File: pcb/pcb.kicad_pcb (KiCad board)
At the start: 2 copper layers, 84.6 x 82.7 mm, 329 parts, among them J1 SMA, J2 SMA, J3 SMA, P1 CONN_02X03, P10 TST, P11 EPV, P12 EPV, P2 A1, P3 SWD, P4 SWC, P5 USB_OTG, P6 CONN_02X03, P7 EPV, P8 TST, P9 TST, Q1 2N7000, Q2 BF861, U1 LM7705, U10 TPS77001DBVT, U11 AD829, U12 AD8061, U13 AD8031, U2 MAX4477, U3 NCP700B, U4 MAX11102, U5 MAX6126BASA25+, U6 STM32F302KxU, U7 NCP700B, U8 501HCA12M0000DAG, U9 LT3571

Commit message: pcb: Update to v1.1
Changes:
 Add input protection diodes to acquisition board
 Add second screw hole to the preamplifier
 Add PCB revision number to the board
 LPF->HPF at the output of the preamplifier board
 Fix connector orientation on the preamplifier board
 Fix enclosure front/back PCBs
 Add constant amplification resistor to the acquisition board
 Switch the reference to 2.0V because MAX4477 has low maximal input common mode
 voltage
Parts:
- removed the REF**11112 at (25.5, 15.8)
- removed the REF**11112 at (27.0, 15.8)
- removed the REF**11113 at (25.5, 17.4)
- removed the REF**11113 at (27.0, 17.4)
- removed the REF**11114 at (27.0, 18.9)
- removed the REF**11114 at (25.5, 18.9)
- removed the REF**11122 at (28.5, 15.8)
- removed the REF**11123 at (28.5, 17.4)
- removed the REF**11124 at (28.5, 18.9)
- removed the REF**11144 at (65.2, 17.8)
- added D3: BAT54S-7-F, TO_SOT_Packages_SMD:SOT-23, B.Cu at (65.8, 18.7)
- added P8: TST, Measurement_Points:Measurement_Point_Round-TH_Big, F.Cu at (27.1, 17.1)
- added R51: 10k, Resistors_SMD:R_0402, F.Cu at (65.0, 21.4)
- added R52: 5k1, Resistors_SMD:R_0402, F.Cu at (69.3, 17.0)
- added REF**11144: VIA, footprints:VIA, F.Cu at (64.7, 16.4)
- added REF**11144: VIA, footprints:VIA, F.Cu at (81.1, 17.9)
- added REF**11144: VIA, footprints:VIA, F.Cu at (79.6, 17.9)
- added REF**11144: VIA, footprints:VIA, F.Cu at (76.6, 17.9)
- added REF**11144: VIA, footprints:VIA, F.Cu at (78.1, 17.9)
- added REF**11144: VIA, footprints:VIA, F.Cu at (76.6, 16.5)
- C49: value 2n2 -> 10n
- C61: value 2n2 -> 100n
- R23: value 20k1 -> 20k
- R3: value 1k -> 1k5
- R35: value 390k -> 510k
- R36: value 154k -> 200k
- R38, R44: value R -> 1k
- R40: value R -> 10k
- R46: value R -> 2k
- R48: value 1k -> 2k
- moved R1 3.73 mm to (65.6, 23.0), turned to 270 degrees
- moved REF** 2.83 mm to (29.4, 65.9)
- moved REF** 2.83 mm to (35.4, 65.9)
- moved REF** 2.83 mm to (29.4, 88.4)
- moved REF** 2.83 mm to (35.4, 88.4)
- moved REF** 2.76 mm to (71.7, 88.4)
- moved REF** 2.76 mm to (77.7, 88.4)
- moved REF** 2.72 mm to (101.6, 65.9)
- moved REF** 2.72 mm to (95.6, 65.9)
- moved C61 2.58 mm to (47.8, 23.5), turned to 180 degrees
- moved REF** 1.65 mm to (79.2, 81.8)
- moved REF** 1.65 mm to (36.9, 81.8)
- moved REF** 1.60 mm to (36.9, 59.4)
- moved REF**11144 1.43 mm to (63.4, 19.2)
- moved C7 1.24 mm to (64.2, 23.0), turned to 270 degrees
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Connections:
- C61 pad 2: GND -> Net-(C59-Pad1)
- JP2 pad 1: Net-(C7-Pad1) -> Net-(D3-Pad3)
- R48 pad 1: SIG -> GND
- R48 pad 2: Net-(C59-Pad1) -> SIG
- U2 pad 3: Net-(C7-Pad1) -> Net-(D3-Pad3)
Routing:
- net /acq_adc/+3.3V_A: track 35.6 -> 44.5 mm
- net V-: track 98.9 -> 106.2 mm
- net Net-(D3-Pad3): track 0.00 -> 4.94 mm, vias 0 -> 1
- net Net-(C7-Pad1): track 0.00 -> 2.72 mm
- net BIAS: track 91.1 -> 88.7 mm, vias 3 -> 5
- net Net-(C59-Pad1): track 10.1 -> 8.27 mm
- net SIG: track 15.9 -> 17.7 mm
- net Net-(R3-Pad2): track 4.74 -> 6.14 mm
- removed copper zone on F.Cu, net Net-(C7-Pad1)
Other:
- outline, holes or cut-outs redrawn
- board text added: "v1.1"

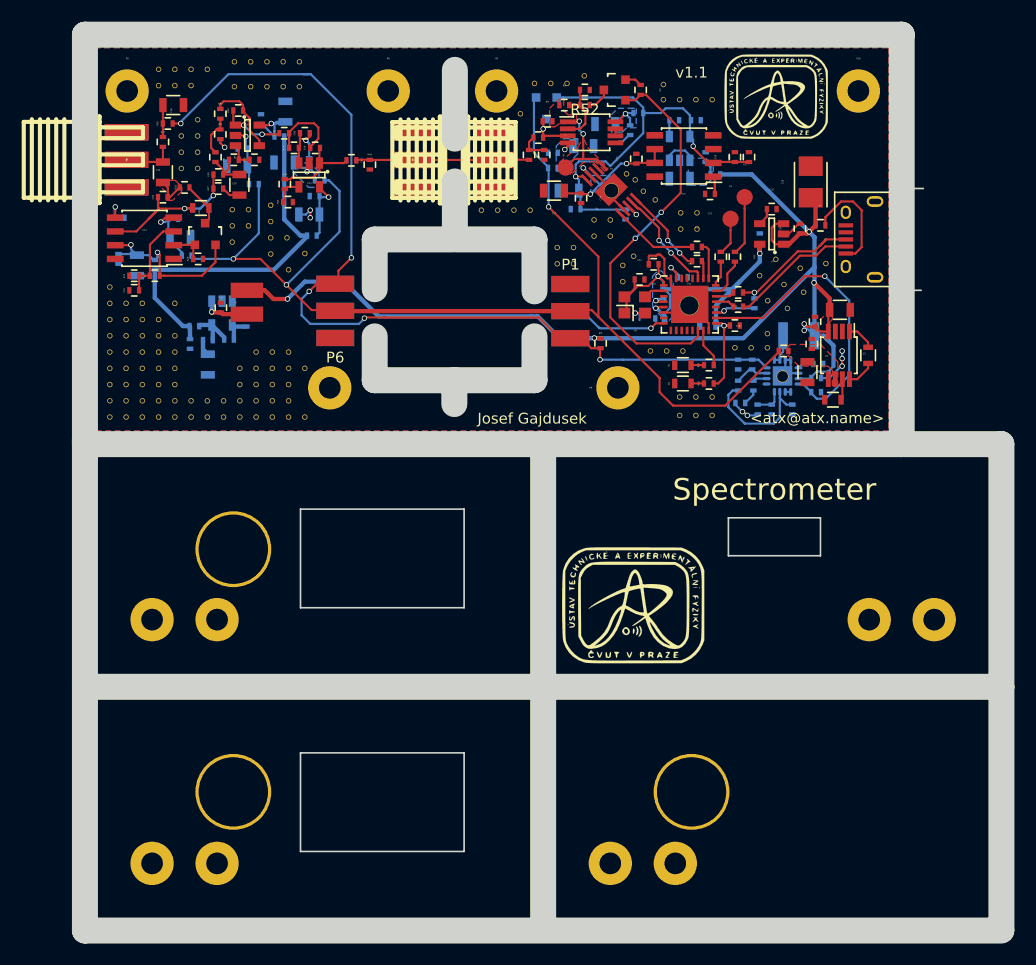
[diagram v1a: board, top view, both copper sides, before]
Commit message: pcb: Update to the current iteration
Looks like I forgot to commit the changes made for manufacturing...
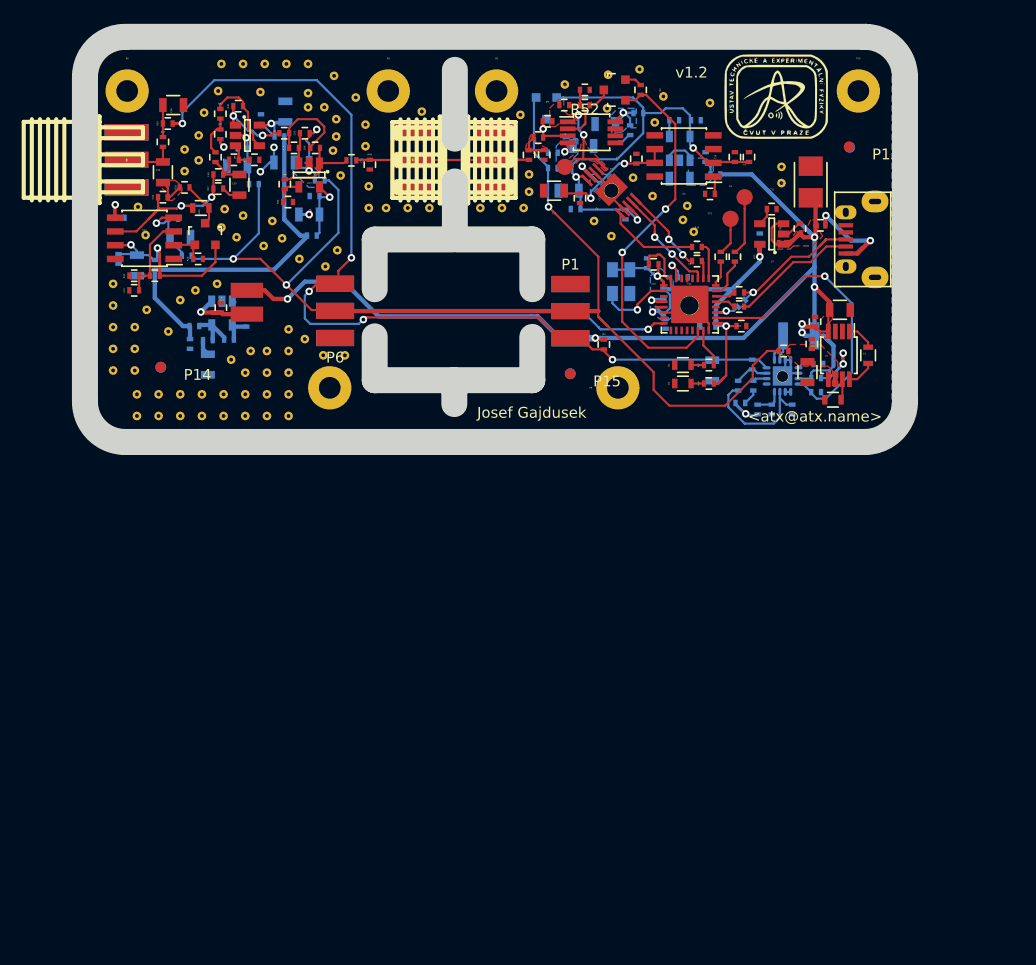
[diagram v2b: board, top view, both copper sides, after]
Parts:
- removed the G*** at (73.8, 64.5)
- removed the REF** at (29.4, 65.9)
- removed the REF** at (101.6, 65.9)
- removed the REF** at (95.6, 65.9)
- removed the REF** at (36.9, 59.4)
- removed the REF** at (36.9, 81.8)
- removed the REF** at (79.2, 81.8)
- removed the REF** at (35.4, 65.9)
- removed the REF** at (29.4, 88.4)
- removed the REF** at (35.4, 88.4)
- removed the REF** at (71.7, 88.4)
- removed the REF** at (77.7, 88.4)
- removed REF**11111 (x2), REF**11112 (x7), REF**11113 (x6), REF**11114 (x6), REF**11115 (x6), REF**11121, REF**11122 (x11), REF**11123 (x3), REF**11124 (x8), REF**11125 (x4), REF**11132, REF**11133 (x2), REF**11134 (x16), REF**11135 (x14), REF**11141, REF**11143 (x2), REF**11144 (x35), REF**11145 (x31): VIA, footprints:VIA
- added P13: FID, Fiducials:Fiducial_1mm_Dia_2.54mm_Outer_CopperTop, F.Cu at (93.8, 22.2)
- added P14: FID, Fiducials:Fiducial_1mm_Dia_2.54mm_Outer_CopperTop, F.Cu at (30.2, 42.6)
- added P15: FID, Fiducials:Fiducial_1mm_Dia_2.54mm_Outer_CopperTop, F.Cu at (68.0, 43.2)
- added P16: FID, Fiducials:Fiducial_1mm_Dia_2.54mm_Outer_CopperTop, B.Cu at (30.2, 42.6)
- added P17: FID, Fiducials:Fiducial_1mm_Dia_2.54mm_Outer_CopperTop, B.Cu at (93.8, 22.3)
- added P18: FID, Fiducials:Fiducial_1mm_Dia_2.54mm_Outer_CopperTop, B.Cu at (68.0, 43.2)
- added REF**: VIA, footprints:VIA, F.Cu at (80.9, 18.2)
- added REF**: VIA, footprints:VIA, F.Cu at (73.8, 25.1)
- added REF**: VIA, footprints:VIA, F.Cu at (34.0, 45.1)
- added REF**: VIA, footprints:VIA, F.Cu at (32.0, 45.1)
- added REF**: VIA, footprints:VIA, F.Cu at (30.0, 45.1)
- added REF**: VIA, footprints:VIA, F.Cu at (28.0, 45.1)
- added REF**: VIA, footprints:VIA, F.Cu at (71.8, 30.5)
- added REF**: VIA, footprints:VIA, F.Cu at (70.2, 29.1)
- added REF**: VIA, footprints:VIA, F.Cu at (37.2, 30.6)
- added REF**: VIA, footprints:VIA, F.Cu at (41.4, 30.7)
- added REF**: VIA, footprints:VIA, F.Cu at (46.5, 31.8)
- added REF**: VIA, footprints:VIA, F.Cu at (67.5, 16.5)
- added REF**: VIA, footprints:VIA, F.Cu at (71.5, 15.6)
- added REF**: VIA, footprints:VIA, F.Cu at (74.4, 15.1)
- added REF**: VIA, footprints:VIA, F.Cu at (76.6, 17.6)
- added REF**: VIA, footprints:VIA, F.Cu at (38.5, 41.1)
- added REF**: VIA, footprints:VIA, F.Cu at (75.8, 20.0)
- added REF**: VIA, footprints:VIA, F.Cu at (71.4, 18.7)
- added REF**: VIA, footprints:VIA, F.Cu at (63.4, 19.3)
- added REF**: VIA, footprints:VIA, F.Cu at (64.2, 24.8)
- added REF**: VIA, footprints:VIA, F.Cu at (64.2, 26.4)
- added REF**: VIA, footprints:VIA, F.Cu at (63.7, 27.9)
- added REF**: VIA, footprints:VIA, F.Cu at (59.7, 27.9)
- added REF**: VIA, footprints:VIA, F.Cu at (61.7, 27.9)
- added REF**: VIA, footprints:VIA, F.Cu at (54.3, 19.0)
- added REF**: VIA, footprints:VIA, F.Cu at (49.4, 25.9)
- added REF**: VIA, footprints:VIA, F.Cu at (36.7, 41.9)
- added REF**: VIA, footprints:VIA, F.Cu at (49.4, 27.9)
- added REF**: VIA, footprints:VIA, F.Cu at (55.0, 27.9)
- added REF**: VIA, footprints:VIA, F.Cu at (53.0, 27.9)
- added REF**: VIA, footprints:VIA, F.Cu at (51.0, 27.9)
- added REF**: VIA, footprints:VIA, F.Cu at (46.2, 15.7)
- added REF**: VIA, footprints:VIA, F.Cu at (48.2, 17.7)
- added REF**: VIA, footprints:VIA, F.Cu at (49.1, 20.2)
- added REF**: VIA, footprints:VIA, F.Cu at (49.1, 22.2)
- added REF**: VIA, footprints:VIA, F.Cu at (46.1, 22.6)
- added REF**: VIA, footprints:VIA, F.Cu at (46.4, 21.3)
- added REF**: VIA, footprints:VIA, F.Cu at (87.5, 25.6)
- added REF**: VIA, footprints:VIA, F.Cu at (46.4, 19.7)
- added REF**: VIA, footprints:VIA, F.Cu at (45.3, 18.6)
- added REF**: VIA, footprints:VIA, F.Cu at (43.8, 18.6)
- added REF**: VIA, footprints:VIA, F.Cu at (43.8, 17.3)
- added REF**: VIA, footprints:VIA, F.Cu at (35.5, 17.1)
- added REF**: VIA, footprints:VIA, F.Cu at (39.4, 17.2)
- added REF**: VIA, footprints:VIA, F.Cu at (46.8, 24.9)
- added REF**: VIA, footprints:VIA, F.Cu at (43.5, 40.0)
- added REF**: VIA, footprints:VIA, F.Cu at (47.2, 41.5)
- added REF**: VIA, footprints:VIA, F.Cu at (45.2, 41.5)
- added REF**: VIA, footprints:VIA, F.Cu at (78.4, 29.0)
- added REF**: VIA, footprints:VIA, F.Cu at (45.4, 33.3)
- added REF**: VIA, footprints:VIA, F.Cu at (43.0, 32.6)
- added REF**: VIA, footprints:VIA, F.Cu at (40.5, 29.1)
- added REF**: VIA, footprints:VIA, F.Cu at (39.7, 31.4)
- added REF**: VIA, footprints:VIA, F.Cu at (35.8, 14.6)
- added REF**: VIA, footprints:VIA, F.Cu at (39.8, 14.6)
- added REF**: VIA, footprints:VIA, F.Cu at (37.8, 14.6)
- added REF**: VIA, footprints:VIA, F.Cu at (43.8, 14.6)
- added REF**: VIA, footprints:VIA, F.Cu at (41.8, 14.6)
- added REF**: VIA, footprints:VIA, F.Cu at (34.2, 19.1)
- added REF**: VIA, footprints:VIA, F.Cu at (87.5, 24.1)
- added REF**: VIA, footprints:VIA, F.Cu at (33.7, 23.5)
- added REF**: VIA, footprints:VIA, F.Cu at (33.7, 21.2)
- added REF**: VIA, footprints:VIA, F.Cu at (32.4, 22.5)
- added REF**: VIA, footprints:VIA, F.Cu at (32.4, 24.5)
- added REF**: VIA, footprints:VIA, F.Cu at (33.4, 35.5)
- added REF**: VIA, footprints:VIA, F.Cu at (35.4, 34.9)
- added REF**: VIA, footprints:VIA, F.Cu at (37.8, 28.6)
- added REF**: VIA, footprints:VIA, F.Cu at (35.8, 29.7)
- added REF**: VIA, footprints:VIA, F.Cu at (36.1, 28.0)
- added REF**: VIA, footprints:VIA, F.Cu at (28.8, 30.4)
- added REF**: VIA, footprints:VIA, F.Cu at (78.8, 27.7)
- added REF**: VIA, footprints:VIA, F.Cu at (28.1, 27.8)
- added REF**: VIA, footprints:VIA, F.Cu at (32.0, 36.4)
- added REF**: VIA, footprints:VIA, F.Cu at (30.9, 39.3)
- added REF**: VIA, footprints:VIA, F.Cu at (28.9, 37.3)
- added REF**: VIA, footprints:VIA, F.Cu at (25.8, 36.9)
- added REF**: VIA, footprints:VIA, F.Cu at (25.8, 34.9)
- added REF**: VIA, footprints:VIA, F.Cu at (27.8, 38.9)
- added REF**: VIA, footprints:VIA, F.Cu at (25.8, 40.9)
- added REF**: VIA, footprints:VIA, F.Cu at (27.8, 40.9)
- added REF**: VIA, footprints:VIA, F.Cu at (25.8, 38.9)
- added REF**: VIA, footprints:VIA, F.Cu at (79.4, 30.1)
- added REF**: VIA, footprints:VIA, F.Cu at (25.8, 42.9)
- added REF**: VIA, footprints:VIA, F.Cu at (27.8, 42.9)
- added REF**: VIA, footprints:VIA, F.Cu at (42.0, 39.1)
- added REF**: VIA, footprints:VIA, F.Cu at (42.0, 41.1)
- added REF**: VIA, footprints:VIA, F.Cu at (40.0, 41.1)
- added REF**: VIA, footprints:VIA, F.Cu at (38.0, 43.1)
- added REF**: VIA, footprints:VIA, F.Cu at (42.0, 43.1)
- added REF**: VIA, footprints:VIA, F.Cu at (40.0, 43.1)
- added REF**: VIA, footprints:VIA, F.Cu at (38.0, 47.1)
- added REF**: VIA, footprints:VIA, F.Cu at (38.0, 45.1)
- added REF**: VIA, footprints:VIA, F.Cu at (75.6, 26.8)
- added REF**: VIA, footprints:VIA, F.Cu at (42.0, 47.1)
- added REF**: VIA, footprints:VIA, F.Cu at (40.0, 47.1)
- added REF**: VIA, footprints:VIA, F.Cu at (42.0, 45.1)
- added REF**: VIA, footprints:VIA, F.Cu at (40.0, 45.1)
- added REF**: VIA, footprints:VIA, F.Cu at (36.0, 47.1)
- added REF**: VIA, footprints:VIA, F.Cu at (34.0, 47.1)
- added REF**: VIA, footprints:VIA, F.Cu at (32.0, 47.1)
- added REF**: VIA, footprints:VIA, F.Cu at (30.0, 47.1)
- added REF**: VIA, footprints:VIA, F.Cu at (28.0, 47.1)
- added REF**: VIA, footprints:VIA, F.Cu at (36.0, 45.1)
- C31: moved to B.Cu
- C36: value 100n -> 100n/200V; footprint Resistors_SMD:R_0402 -> Resistors_SMD:R_0805
- C49: value 10n -> 1n
- JP2, JP3, JP5: value Jumper_NO_Small -> DNP
- JP4, JP6: value Jumper_NC_Small -> 0R
- L4: value BEAD -> BLM15AX121SN1D
- P5: footprint Connect:USB_Micro-B -> footprints:USB_Micro-B
- Q1: value 2N7000 -> BSS138
- R39: value 1k -> 5k1
- U1: value LM7705 -> LM7705MM
- U11: value AD829 -> AD829ARZ
- U12: value AD8061 -> AD8061ARTZ
- U13: value AD8031 -> AD8031ARTZ
- U2: value MAX4477 -> MAX4477AUA+
- U3, U7: value NCP700B -> NCP700BSN33T1G
- U4: value MAX11102 -> MAX11102AUB+
- U5: value MAX6126BASA25+ -> MAX6126BASA21+
- U6: value STM32F302KxU -> STM32F302K8U6
- U8: value 501HCA12M0000DAG -> QX333A12.00000B15M; footprint footprints:501HCA_2.5x2 -> footprints:QX333A; moved to B.Cu
- U9: value LT3571 -> LT3571EUD
- moved U8 2.56 mm to (72.7, 34.7), turned to 270 degrees
- moved C36 2.46 mm to (81.1, 42.9)
- moved C31 1.66 mm to (75.1, 33.0), turned to 90 degrees
- moved R16 1.20 mm to (83.8, 36.7), turned to 225 degrees
- moved C27 0.71 mm to (76.8, 38.6), turned to 270 degrees
- moved C26 0.60 mm to (83.8, 38.8)
- moved R40 0.40 mm to (37.4, 18.5)
- moved JP3 0.32 mm to (71.1, 40.5)
- moved C19 0.10 mm to (68.9, 27.0)
- moved R14 0.10 mm to (83.6, 37.0)
- moved R15 0.10 mm to (83.6, 35.7)
- moved P2 0.10 mm to (67.5, 24.1)
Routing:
- net (no net): track 48.2 -> 0.00 mm
- net GND: track 44.6 -> 52.3 mm, vias 10 -> 8
- net /acq_mcu/CLK: track 3.07 -> 6.90 mm, vias 0 -> 1
- net V-: track 106.2 -> 109.9 mm
- net /acq_adc/REF: track 14.2 -> 17.6 mm
- net +3V3: track 45.4 -> 48.7 mm
- net Net-(C45-Pad1): track 16.5 -> 19.7 mm
- net Net-(C46-Pad1): track 2.02 -> 4.43 mm
- net Net-(R40-Pad1): track 5.88 -> 8.20 mm
- net Net-(C40-Pad1): track 4.34 -> 6.57 mm
- net /acq_adc/+3.3V_A: track 44.5 -> 46.6 mm
- net Net-(C42-Pad1): track 6.11 -> 8.21 mm
- net Net-(L2-Pad2): track 2.85 -> 4.91 mm
- net /acq_adc/AMP_x: track 36.6 -> 35.2 mm
- net Net-(C59-Pad2): track 6.84 -> 8.21 mm
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- added copper zone on F.Cu, net Net-(C7-Pad1)
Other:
- board size 84.6 x 82.7 mm -> 75.7 x 37.4 mm
- net class Default: via_dia 0.5 -> 0.7
- rule via_min_size: 0.4 -> 0.7
- board text added: "v1.2"
- board text removed: "Spectrometer"
- board text removed: "v1.1"
